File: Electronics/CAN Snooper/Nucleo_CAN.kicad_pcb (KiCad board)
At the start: 2 copper layers, 57.8 x 50.8 mm, 39 parts, among them J1 CAN_In, J2 CAN_Out, SW1 Reset, T1 12V Iso Test, T10 CAN L Test, T11 CAN Output GND Test, T2 5V Iso Test, T3 9V Test, T4 3.3V Test, T5 CAN PwrSense Test, T6 CAN Tx Test, T7 CAN Rx Test, T8 CAN Input GND Test, T9 CAN H Test, U1 PDS1-S12-S9-M, U2 MCP1702T-5002E/CB, U3 Nucleo_L432KC, U4 ADM3054

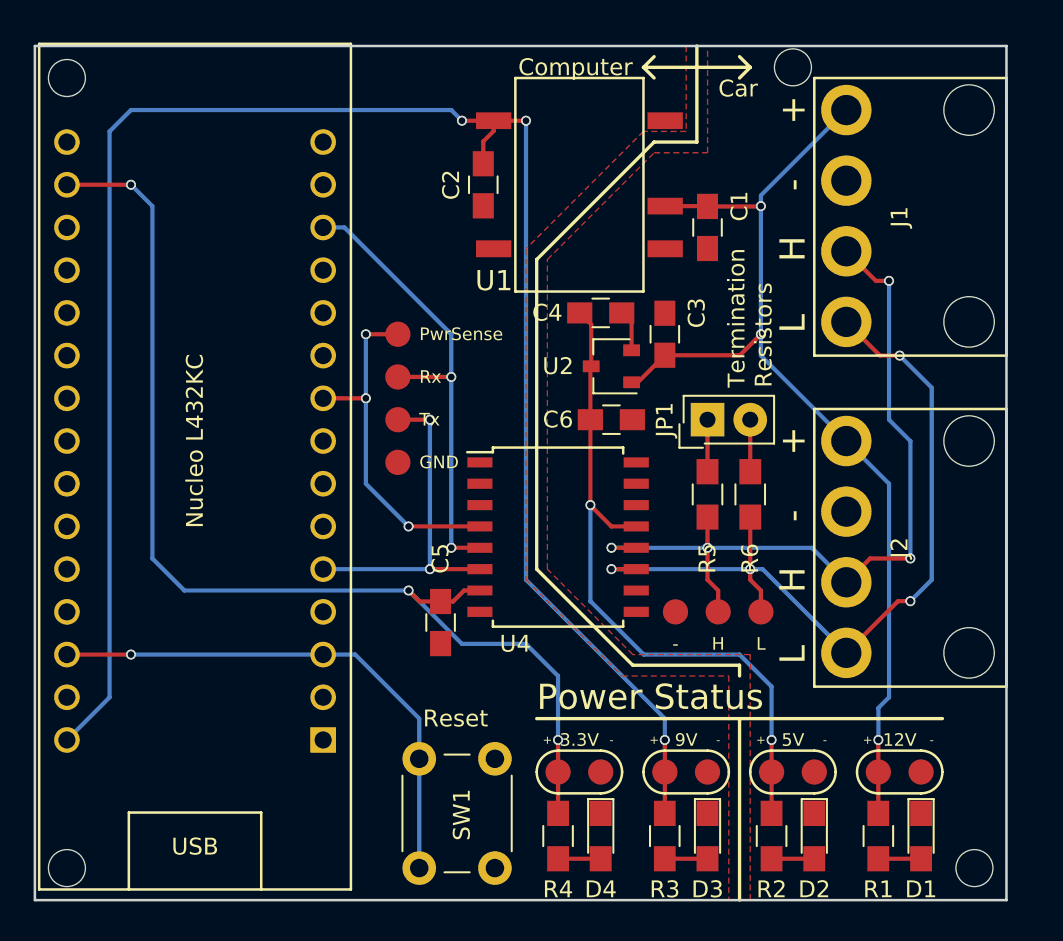
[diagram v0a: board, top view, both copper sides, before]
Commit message: CAN Snooper: PCB: Rearranged screw holes and stretched board
In order to give the mounting screws proper clearance and to fully
contain the screw heads on top of the board, I moved the screw holes
around and stretched the board size by approximately 0.16 sq.in.
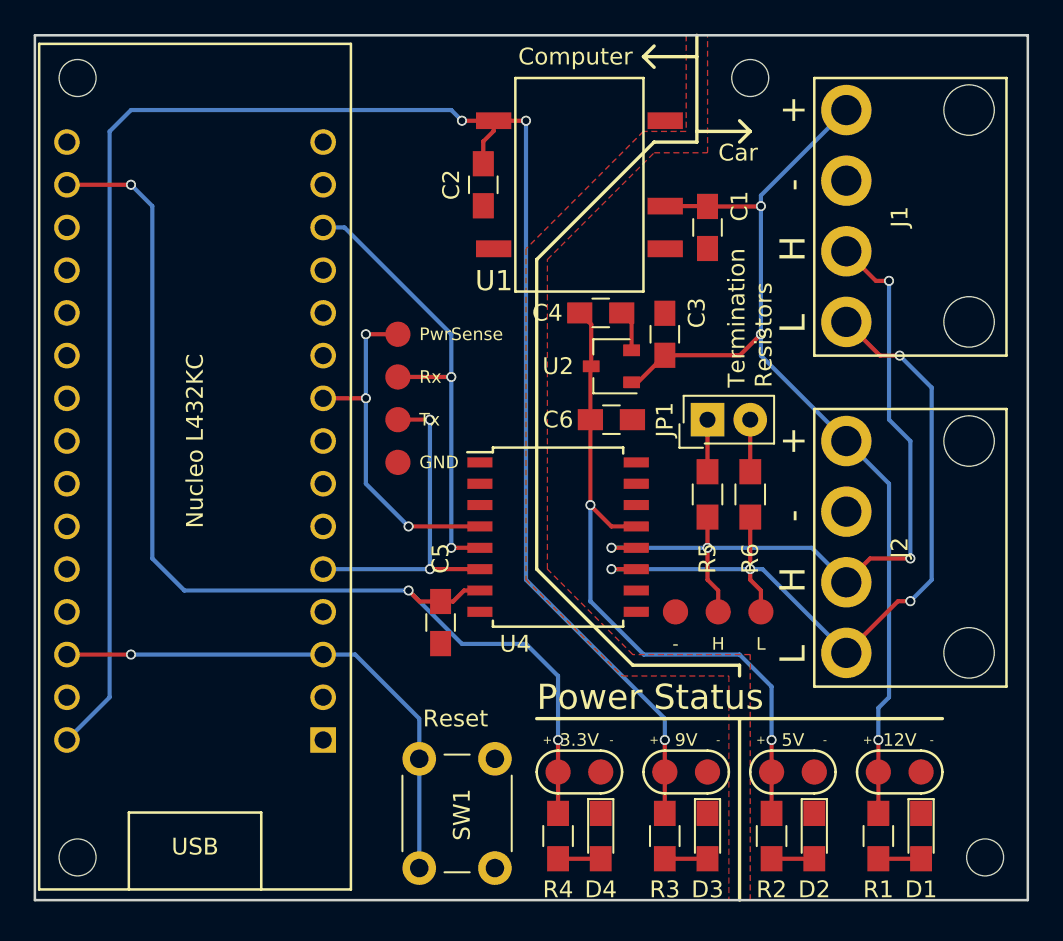
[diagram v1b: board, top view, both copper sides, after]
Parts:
- moved REF** 2.62 mm to (199.4, 53.3)
- moved REF** 0.90 mm to (213.4, 99.7)
- moved REF** 0.90 mm to (159.4, 99.7)
- moved REF** 0.63 mm to (159.4, 53.3)
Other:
- board size 57.8 x 50.8 mm -> 59.1 x 51.4 mm
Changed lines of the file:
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@@
   )
   (module Custom:MountingHole-M2-nonplated (layer F.Cu)
-    (at 158.75 53.34)
+    (at 159.385 53.34)
     (fp_text reference REF** (at 0 1.905) (layer F.SilkS) hide
       (effects (font (size 1 1) (thickness 0.15)))
@@
   )
   (module Custom:MountingHole-M2-nonplated (layer F.Cu)
-    (at 158.75 100.33)
+    (at 159.385 99.695)
     (fp_text reference REF** (at 0 1.905) (layer F.SilkS) hide
       (effects (font (size 1 1) (thickness 0.15)))
@@
   )
   (module Custom:MountingHole-M2-nonplated (layer F.Cu)
-    (at 212.725 100.33)
+    (at 213.36 99.695)
     (fp_text reference REF** (at 0 1.905) (layer F.SilkS) hide
       (effects (font (size 1 1) (thickness 0.15)))
@@
   )
   (module Custom:MountingHole-M2-nonplated (layer F.Cu)
-    (at 201.93 52.705)
+    (at 199.39 53.34)
     (fp_text reference REF** (at 0 1.905) (layer F.SilkS) hide
       (effects (font (size 1 1) (thickness 0.15)))
@@
       (net 3 +9V))
   )
-  (gr_circle (center 201.93 52.705) (end 201.93 54.905) (layer Dwgs.User) (width 0.2))
-  (gr_circle (center 212.725 100.33) (end 212.725 102.53) (layer Dwgs.User) (width 0.2))
-  (gr_circle (center 158.75 100.33) (end 158.75 102.53) (layer Dwgs.User) (width 0.2))
-  (gr_circle (center 158.75 53.34) (end 158.75 55.54) (layer Dwgs.User) (width 0.2))
-  (dimension 57.785 (width 0.3) (layer Eco1.User)
-    (gr_text "2.2750 in" (at 185.7375 48.815) (layer Eco1.User)
+  (dimension 51.435 (width 0.3) (layer Dwgs.User)
+    (gr_text "2.0250 in" (at 154.225 76.5175 90) (layer Dwgs.User)
       (effects (font (size 1.5 1.5) (thickness 0.3)))
     )
-    (feature1 (pts (xy 214.63 51.435) (xy 214.63 47.465)))
-    (feature2 (pts (xy 156.845 51.435) (xy 156.845 47.465)))
-    (crossbar (pts (xy 156.845 50.165) (xy 214.63 50.165)))
-    (arrow1a (pts (xy 214.63 50.165) (xy 213.503496 50.751421)))
-    (arrow1b (pts (xy 214.63 50.165) (xy 213.503496 49.578579)))
-    (arrow2a (pts (xy 156.845 50.165) (xy 157.971504 50.751421)))
-    (arrow2b (pts (xy 156.845 50.165) (xy 157.971504 49.578579)))
-  )
+    (feature1 (pts (xy 156.845 50.8) (xy 152.875 50.8)))
+    (feature2 (pts (xy 156.845 102.235) (xy 152.875 102.235)))
+    (crossbar (pts (xy 155.575 102.235) (xy 155.575 50.8)))
+    (arrow1a (pts (xy 155.575 50.8) (xy 156.161421 51.926504)))
+    (arrow1b (pts (xy 155.575 50.8) (xy 154.988579 51.926504)))
+    (arrow2a (pts (xy 155.575 102.235) (xy 156.161421 101.108496)))
+    (arrow2b (pts (xy 155.575 102.235) (xy 154.988579 101.108496)))
+  )
+  (dimension 59.055 (width 0.3) (layer Dwgs.User)
+    (gr_text "2.3250 in" (at 186.3725 48.18) (layer Dwgs.User)
+      (effects (font (size 1.5 1.5) (thickness 0.3)))
+    )
+    (feature1 (pts (xy 215.9 50.8) (xy 215.9 46.83)))
+    (feature2 (pts (xy 156.845 50.8) (xy 156.845 46.83)))
+    (crossbar (pts (xy 156.845 49.53) (xy 215.9 49.53)))
+    (arrow1a (pts (xy 215.9 49.53) (xy 214.773496 50.116421)))
+    (arrow1b (pts (xy 215.9 49.53) (xy 214.773496 48.943579)))
+    (arrow2a (pts (xy 156.845 49.53) (xy 157.971504 50.116421)))
+    (arrow2b (pts (xy 156.845 49.53) (xy 157.971504 48.943579)))
+  )
+  (gr_circle (center 199.39 53.34) (end 199.39 55.54) (layer Dwgs.User) (width 0.2))
+  (gr_circle (center 213.36 99.695) (end 213.36 101.895) (layer Dwgs.User) (width 0.2))
+  (gr_circle (center 159.385 99.695) (end 159.385 101.895) (layer Dwgs.User) (width 0.2))
+  (gr_circle (center 159.385 53.34) (end 159.385 55.54) (layer Dwgs.User) (width 0.2))
   (gr_text L (at 201.93 67.945 90) (layer F.SilkS)
     (effects (font (size 1.5 1.5) (thickness 0.3)))
@@
     (effects (font (size 0.75 0.75) (thickness 0.1875)) (justify left))
   )
-  (dimension 50.8 (width 0.3) (layer Eco1.User)
-    (gr_text "2.0000 in" (at 154.225 76.835 90) (layer Eco1.User)
-      (effects (font (size 1.5 1.5) (thickness 0.3)))
-    )
-    (feature1 (pts (xy 156.845 51.435) (xy 152.875 51.435)))
-    (feature2 (pts (xy 156.845 102.235) (xy 152.875 102.235)))
-    (crossbar (pts (xy 155.575 102.235) (xy 155.575 51.435)))
-    (arrow1a (pts (xy 155.575 51.435) (xy 156.161421 52.561504)))
-    (arrow1b (pts (xy 155.575 51.435) (xy 154.988579 52.561504)))
-    (arrow2a (pts (xy 155.575 102.235) (xy 156.161421 101.108496)))
-    (arrow2b (pts (xy 155.575 102.235) (xy 154.988579 101.108496)))
-  )
   (gr_text H (at 201.93 83.185 90) (layer F.SilkS)
     (effects (font (size 1.5 1.5) (thickness 0.3)))
   )
-  (gr_line (start 214.63 102.235) (end 156.845 102.235) (angle 90) (layer Edge.Cuts) (width 0.15))
-  (gr_line (start 156.845 51.435) (end 214.63 51.435) (angle 90) (layer Edge.Cuts) (width 0.15))
-  (gr_line (start 156.845 102.235) (end 156.845 51.435) (angle 90) (layer Edge.Cuts) (width 0.15))
-  (gr_line (start 214.63 51.435) (end 214.63 102.235) (angle 90) (layer Edge.Cuts) (width 0.15))
+  (gr_line (start 215.9 102.235) (end 156.845 102.235) (angle 90) (layer Edge.Cuts) (width 0.15))
+  (gr_line (start 156.845 50.8) (end 215.9 50.8) (angle 90) (layer Edge.Cuts) (width 0.15))
+  (gr_line (start 156.845 102.235) (end 156.845 50.8) (angle 90) (layer Edge.Cuts) (width 0.15))
+  (gr_line (start 215.9 50.8) (end 215.9 102.235) (angle 90) (layer Edge.Cuts) (width 0.15))
   (gr_line (start 198.755 88.265) (end 198.755 88.9) (angle 90) (layer F.SilkS) (width 0.2))
   (gr_line (start 192.405 88.265) (end 198.755 88.265) (angle 90) (layer F.SilkS) (width 0.2))
@@
   )
   (gr_line (start 186.69 82.55) (end 186.69 64.135) (angle 90) (layer F.SilkS) (width 0.2))
-  (gr_line (start 196.215 57.15) (end 196.215 51.435) (angle 90) (layer F.SilkS) (width 0.2))
+  (gr_line (start 196.215 57.15) (end 196.215 50.8) (angle 90) (layer F.SilkS) (width 0.2))
   (gr_line (start 193.675 57.15) (end 196.215 57.15) (angle 90) (layer F.SilkS) (width 0.2))
   (gr_line (start 186.69 64.135) (end 193.675 57.15) (angle 90) (layer F.SilkS) (width 0.2))
-  (gr_text Car (at 197.485 53.975) (layer F.SilkS)
+  (gr_text Car (at 197.485 57.785) (layer F.SilkS)
     (effects (font (size 1 1) (thickness 0.2)) (justify left))
   )
-  (gr_text Computer (at 192.405 52.705) (layer F.SilkS)
+  (gr_text Computer (at 192.405 52.07) (layer F.SilkS)
     (effects (font (size 1 1) (thickness 0.2)) (justify right))
   )
-  (gr_line (start 198.755 53.34) (end 199.39 52.705) (angle 90) (layer F.SilkS) (width 0.2))
-  (gr_line (start 199.39 52.705) (end 198.755 52.07) (angle 90) (layer F.SilkS) (width 0.2))
-  (gr_line (start 196.215 52.705) (end 199.39 52.705) (angle 90) (layer F.SilkS) (width 0.2))
-  (gr_line (start 193.675 53.34) (end 193.04 52.705) (angle 90) (layer F.SilkS) (width 0.2))
-  (gr_line (start 193.04 52.705) (end 193.675 52.07) (angle 90) (layer F.SilkS) (width 0.2))
-  (gr_line (start 196.215 52.705) (end 193.04 52.705) (angle 90) (layer F.SilkS) (width 0.2))
+  (gr_line (start 198.755 57.15) (end 199.39 56.515) (angle 90) (layer F.SilkS) (width 0.2))
+  (gr_line (start 199.39 56.515) (end 198.755 55.88) (angle 90) (layer F.SilkS) (width 0.2))
+  (gr_line (start 196.215 56.515) (end 199.39 56.515) (angle 90) (layer F.SilkS) (width 0.2))
+  (gr_line (start 193.675 52.705) (end 193.04 52.07) (angle 90) (layer F.SilkS) (width 0.2))
+  (gr_line (start 193.04 52.07) (end 193.675 51.435) (angle 90) (layer F.SilkS) (width 0.2))
+  (gr_line (start 196.215 52.07) (end 193.04 52.07) (angle 90) (layer F.SilkS) (width 0.2))
   (gr_text Reset (at 181.864 91.44) (layer F.SilkS)
     (effects (font (size 1 1) (thickness 0.2)))
@@
     (polygon
       (pts
-        (xy 214.63 102.235) (xy 199.39 102.235) (xy 199.39 87.63) (xy 192.405 87.63) (xy 187.325 82.55)
-        (xy 187.325 64.135) (xy 193.675 57.785) (xy 196.85 57.785) (xy 196.85 51.435) (xy 214.63 51.435)
+        (xy 215.9 102.235) (xy 199.39 102.235) (xy 199.39 87.63) (xy 192.405 87.63) (xy 187.325 82.55)
+        (xy 187.325 64.135) (xy 193.675 57.785) (xy 196.85 57.785) (xy 196.85 50.8) (xy 215.9 50.8)
       )
     )
@@
       (pts
         (xy 195.58 56.515) (xy 193.04 56.515) (xy 186.055 63.5) (xy 186.055 83.185) (xy 191.77 88.9)
-        (xy 198.12 88.9) (xy 198.12 102.235) (xy 156.845 102.235) (xy 156.845 51.435) (xy 195.58 51.435)
+        (xy 198.12 88.9) (xy 198.12 102.235) (xy 156.845 102.235) (xy 156.845 50.8) (xy 195.58 50.8)
       )
     )
